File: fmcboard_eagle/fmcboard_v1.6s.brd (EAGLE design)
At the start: 147 x 74 mm, 297 parts, among them IC1 OPA699ID, IC10 LM358, IC11 7805DT, IC12 SN74AUC2G66DCTR, IC13 SN74AUC2G66DCTR, IC14 SN74AUC2G66DCTR, IC15 SN74AUC2G66DCTR, IC16 DAC7578SPWR, IC17 SN74AUC2G66DCTR, IC18 SN74AUC2G66DCTR, IC19 SN74AUC2G66DCTR, IC2 DAC7578SPWR, IC20 SN74AUC2G66DCTR, IC21 74AUP2GU04GW, IC22 74AUP2GU04GW, IC23 74AUP2GU04GW, IC24 74AUP2GU04GW, IC25 MC7905ACD2TR4G, IC26 AMS1117-1.8, IC27 LM358, IC28 SN74AUC2G66DCTR, IC29 LM337KVURG3, IC3 LTC6229IMS8E#TRPBF, IC30 SN74AUC2G66DCTR, IC31 SN74AUC2G66DCTR, IC32 SN74AUC2G66DCTR, IC33 LTC6229IMS8E#TRPBF, IC34 74AUP2GU04GW, IC35 74AUP2GU04GW, IC36 TPS5430DDAR, IC37 TPS5430DDAR, IC4 OPA695IDR, IC5 LTC6229IMS8E#TRPBF, IC6 OPA695IDR, IC7 OPA699ID, IC8 LM358, IC9 LM358, J1 8pin, J12 4p-2.54, J13 4p-2.54, J2 ASP-134604-01, J3 2p-2.54, J5 4p-2.54, J8 4p-2.54, J9 2p-2.54

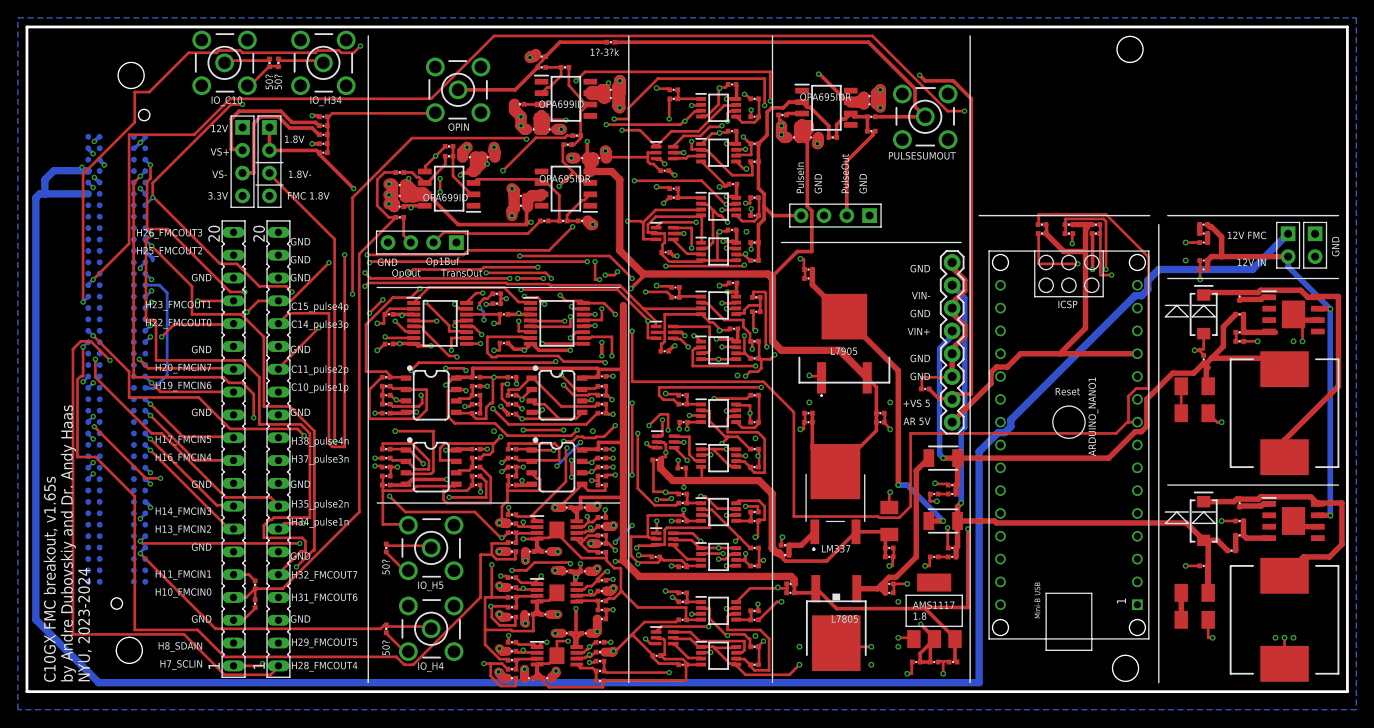
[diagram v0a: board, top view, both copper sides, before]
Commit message: extra 10 uF caps
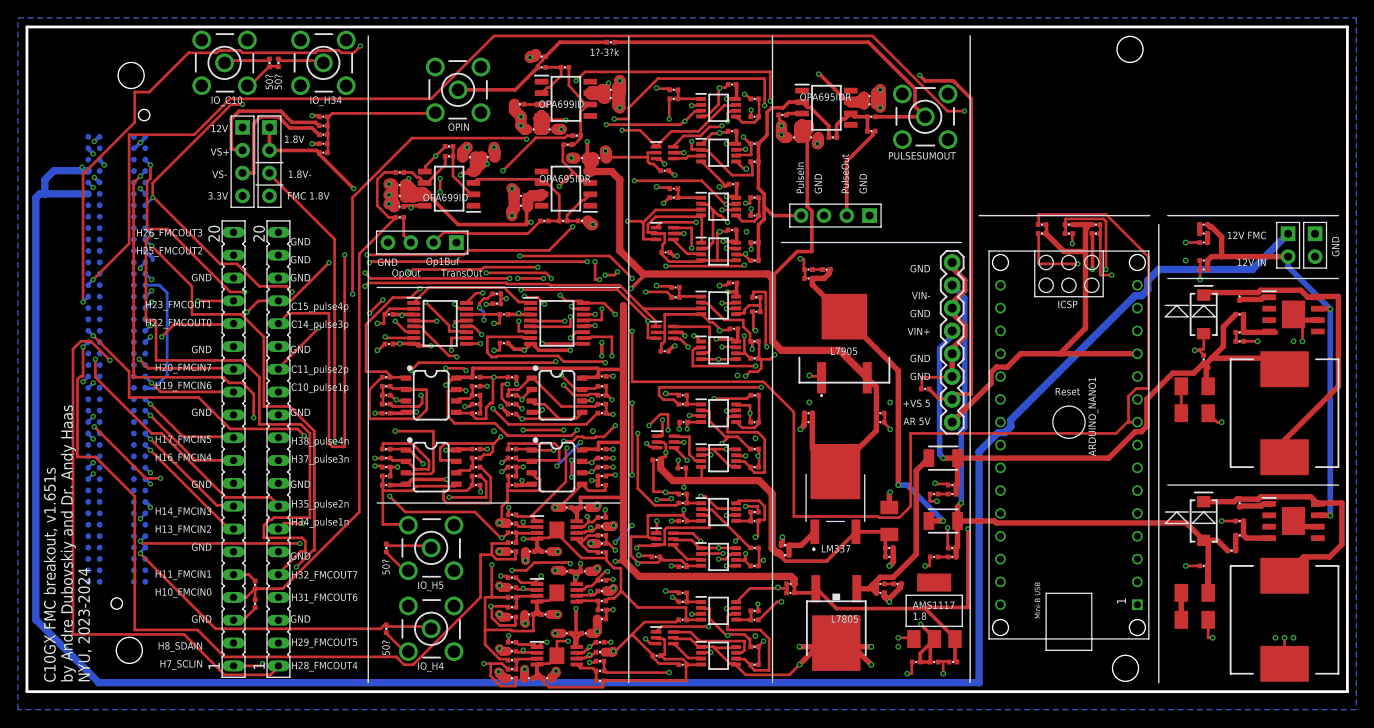
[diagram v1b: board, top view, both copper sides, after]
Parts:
- added C110, C111: 10uF, passives:0402_CAP
- moved C2 1.00 mm to (95.0, 12.0)
- moved C43 1.00 mm to (95.0, 11.0)
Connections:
- new net N$58: C110.1, C2.2
- new net N$59: C111.1, C40.2
- net GND: now also C110.2; no longer C2.2
- net VIN-CLEAN: now also C111.2; no longer C40.2
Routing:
- net GND: track 510.0 -> 529.4 mm, vias 136 -> 135
- net VS-: track 240.4 -> 252.4 mm
- net VIN-CLEAN: track 36.2 -> 37.8 mm
- net N$59: track 0.00 -> 1.13 mm
- net N$58: track 0.00 -> 1.03 mm
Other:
- board text added: "C10GX FMC breakout, v1.651s by Andre Dubovskiy and Dr. Andy Haas NYU, 2023-2024"
- board text removed: "C10GX FMC breakout, v1.65s by Andre Dubovskiy and Dr. Andy Haas NYU, 2023-2024"

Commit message: v1.652s Add C18 C19 C22 C23 pulse out holes Add C26 C27 SDAIN SCLIN holes
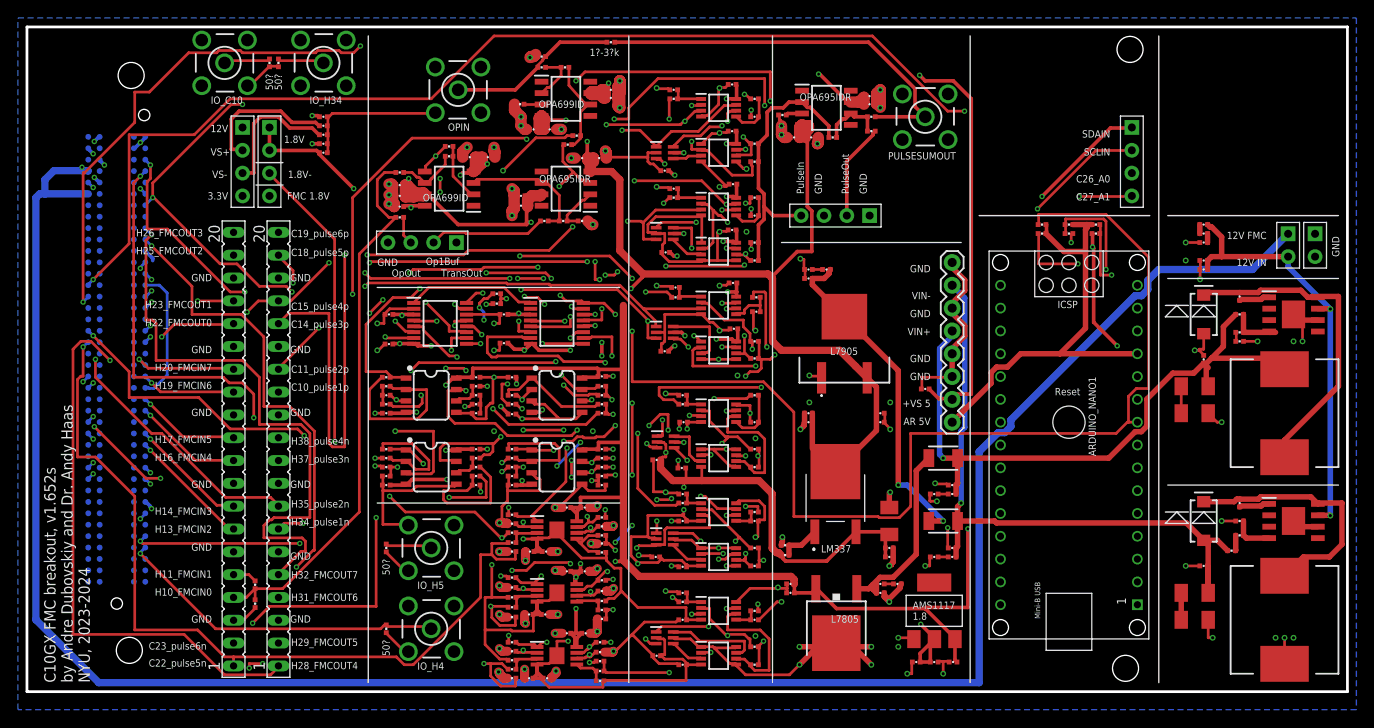
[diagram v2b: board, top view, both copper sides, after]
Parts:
- added J4: 4p-2.54, Seeed-Connector:H4-2.54
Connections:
- net C18: now also SV2.19
- net C19: now also SV2.20
- net C22: now also SV1.1
- net C23: now also SV1.2
- net C26: now also J4.3
- net C27: now also J4.4
- net GND: no longer SV2.19, SV2.20
- net SCLIN: now also J4.2; no longer SV1.1
- net SDAIN: now also J4.1; no longer SV1.2
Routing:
- net C23: track 74.4 -> 105.3 mm, vias 3 -> 5
- net SDAIN: track 153.7 -> 180.0 mm, vias 2 -> 4
- net SCLIN: track 156.9 -> 172.9 mm, vias 3 -> 5
- net C27: track 173.3 -> 181.5 mm, vias 2 -> 3
- net C19: track 85.3 -> 91.1 mm
- net C26: track 183.5 -> 189.0 mm
- net C18: track 76.8 -> 80.9 mm, vias 2 -> 3
- net C22: track 92.5 -> 93.5 mm
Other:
- board text added: "C10GX FMC breakout, v1.652s by Andre Dubovskiy and Dr. Andy Haas NYU, 2023-2024"
- board text added: "C18_pulse5p"
- board text added: "C19_pulse6p"
- board text added: "C22_pulse5n"
- board text added: "C23_pulse6n"
- board text added: "C26_A0"
- board text added: "C27_A1"
- board text added: "SCLIN"
- board text added: "SDAIN"
- board text removed: "C10GX FMC breakout, v1.651s by Andre Dubovskiy and Dr. Andy Haas NYU, 2023-2024"
- board text removed: "H7_SCLIN"
- board text removed: "H8_SDAIN"

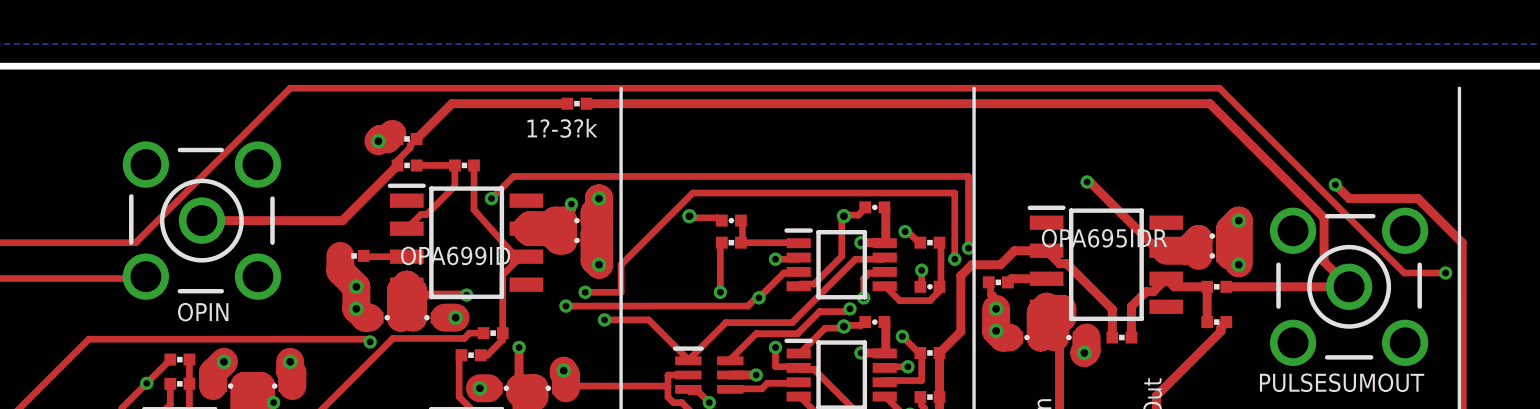
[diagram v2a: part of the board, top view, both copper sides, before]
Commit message: v1.652s 0805 test resistor instead of 0402
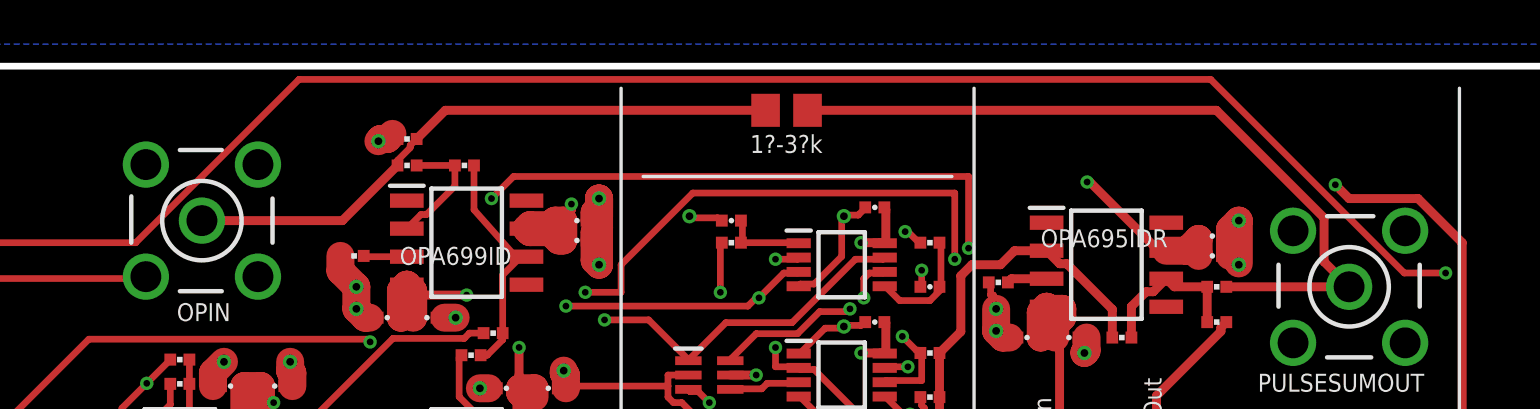
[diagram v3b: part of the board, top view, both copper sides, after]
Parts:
- R9: device passives:0402_RES -> rcl:R0805
- moved R9 9.50 mm to (74.5, 72.0)
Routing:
- net PULSEOUT: track 44.7 -> 34.6 mm
- net IO1: track 19.0 -> 27.8 mm
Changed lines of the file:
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@@
 <text x="120.6" y="57.5" size="0.8128" layer="21" rot="R180">C26_A0</text>
 <text x="120.6" y="55.5" size="0.8128" layer="21" rot="R180">C27_A1</text>
+<wire x1="68" y1="69" x2="82" y2="69" width="0.1524" layer="21"/>
 </plain>
 <attributes>
@@
 <attribute name="VALUE" x="59.5" y="65.4" size="0.8128" layer="21" align="center"/>
 </element>
-<element name="R9" library="passives" package="0402_RES" value="1?-3?k" x="65" y="72.3" smashed="yes">
-<attribute name="VALUE" x="65.932" y="71.581" size="0.8128" layer="21" ratio="15" rot="R180"/>
+<element name="R9" library="rcl" library_urn="urn:adsk.eagle:library:334" package="R0805" package3d_urn="urn:adsk.eagle:package:23553/2" value="1?-3?k" x="74.5" y="72" smashed="yes">
+<attribute name="POPULARITY" value="85" x="74.5" y="72" size="1.778" layer="27" display="off"/>
+<attribute name="SPICEPREFIX" value="R" x="74.5" y="72" size="1.778" layer="27" display="off"/>
+<attribute name="VALUE" x="76.132" y="70.881" size="0.8128" layer="21" ratio="15" rot="R180"/>
 </element>
 <element name="R10" library="passives" package="0402_RES" value="100" x="25.4" y="9.8" smashed="yes" rot="R90"/>
@@
 <wire x1="54.36693125" y1="67" x2="56.86693125" y2="69.5" width="0.4064" layer="1"/>
 <wire x1="48" y1="67" x2="54.36693125" y2="67" width="0.4064" layer="1"/>
-<wire x1="57.73306875" y1="70.7" x2="59.33306875" y2="72.3" width="0.4064" layer="1"/>
-<wire x1="59.33306875" y1="72.3" x2="64.56693125" y2="72.3" width="0.4064" layer="1"/>
+<wire x1="57.73306875" y1="70.7" x2="59.03306875" y2="72" width="0.4064" layer="1"/>
+<wire x1="59.03306875" y1="72" x2="73.55" y2="72" width="0.4064" layer="1"/>
 </signal>
 <signal name="1V8" class="1" airwireshidden="yes">
@@
 <wire x1="98.8656" y1="65.1344" x2="100" y2="64" width="0.4064" layer="1"/>
 <wire x1="98.8656" y1="67.12221875" x2="98.8656" y2="65.1344" width="0.4064" layer="1"/>
-<wire x1="65.43306875" y1="72.3" x2="93.68781875" y2="72.3" width="0.4064" layer="1"/>
-<wire x1="93.68781875" y1="72.3" x2="98.8656" y2="67.12221875" width="0.4064" layer="1"/>
+<wire x1="75.45" y1="72" x2="93.98781875" y2="72" width="0.4064" layer="1"/>
+<wire x1="93.98781875" y1="72" x2="98.8656" y2="67.12221875" width="0.4064" layer="1"/>
 </signal>
 <signal name="TRANSIN">
@@
 <wire x1="22.625" y1="66" x2="18.625" y2="62" width="0.3048" layer="1"/>
 <wire x1="45" y1="66" x2="22.625" y2="66" width="0.3048" layer="1"/>
-<wire x1="52" y1="73" x2="45" y2="66" width="0.3048" layer="1"/>
-<wire x1="94.125" y1="73" x2="52" y2="73" width="0.3048" layer="1"/>
-<wire x1="102.5" y1="64.625" x2="94.125" y2="73" width="0.3048" layer="1"/>
+<wire x1="52.4" y1="73.4" x2="45" y2="66" width="0.3048" layer="1"/>
+<wire x1="93.725" y1="73.4" x2="52.4" y2="73.4" width="0.3048" layer="1"/>
+<wire x1="102.5" y1="64.625" x2="93.725" y2="73.4" width="0.3048" layer="1"/>
 <wire x1="104.375" y1="64.625" x2="102.5" y2="64.625" width="0.3048" layer="1"/>
 <wire x1="122.625" y1="46.375" x2="115.5" y2="53.5" width="0.3048" layer="15"/>

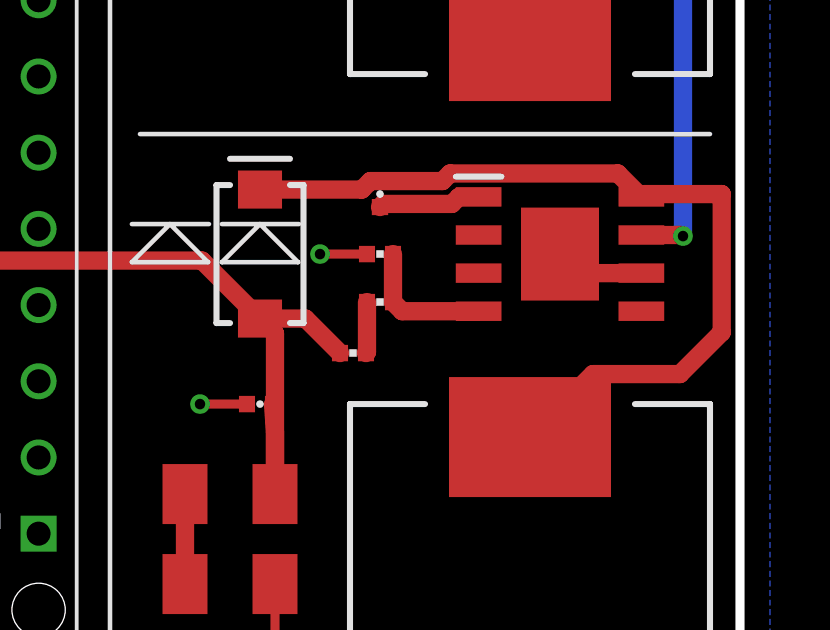
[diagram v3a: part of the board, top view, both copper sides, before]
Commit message: fix VIN-
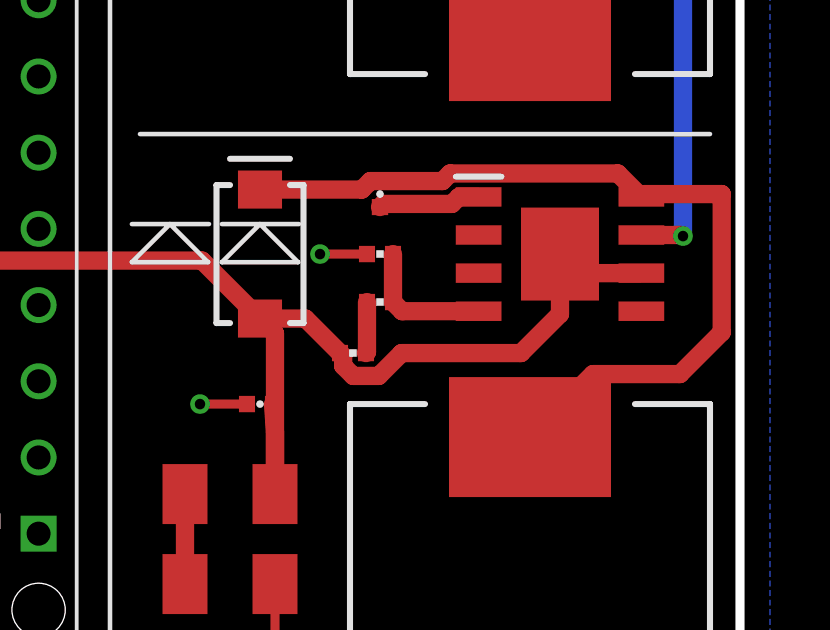
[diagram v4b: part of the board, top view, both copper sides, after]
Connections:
- removed net V-: IC36.6, IC36.9
- net VIN-: now also IC36.6, IC36.9
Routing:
- net VIN-: track 71.7 -> 85.4 mm
- net V-: track 2.98 -> 0.00 mm
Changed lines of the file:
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@@
 <wire x1="104.397" y1="29.4213375" x2="104.397" y2="43.843" width="0.6096" layer="16"/>
 <wire x1="104.397" y1="43.843" x2="103" y2="45.24" width="0.6096" layer="16"/>
+<contactref element="IC36" pad="6"/>
+<contactref element="IC36" pad="9"/>
+<wire x1="143.712" y1="18.365" x2="141.635" y2="18.365" width="0.6096" layer="1"/>
+<wire x1="141.635" y1="18.365" x2="141" y2="19" width="0.6096" layer="1"/>
+<wire x1="133.66693125" y1="15.7" x2="133.77106875" y2="15.5958625" width="0.6096" layer="1"/>
+<wire x1="135.72066875" y1="15.7" x2="139.7" y2="15.7" width="0.6096" layer="1"/>
+<wire x1="133.77106875" y1="15.5958625" x2="133.77106875" y2="15.2744" width="0.6096" layer="1"/>
+<wire x1="133.77106875" y1="15.2744" x2="134.10746875" y2="14.938" width="0.6096" layer="1"/>
+<wire x1="134.10746875" y1="14.938" x2="134.95866875" y2="14.938" width="0.6096" layer="1"/>
+<wire x1="134.95866875" y1="14.938" x2="135.72066875" y2="15.7" width="0.6096" layer="1"/>
+<wire x1="141" y1="17" x2="141" y2="19" width="0.6096" layer="1"/>
+<wire x1="139.7" y1="15.7" x2="141" y2="17" width="0.6096" layer="1"/>
 </signal>
 <signal name="DACP2">
@@
 <via x="59.5" y="35.25" extent="1-16" drill="0.3048"/>
 </signal>
-<signal name="V-">
-<contactref element="IC36" pad="6"/>
-<contactref element="IC36" pad="9"/>
-<wire x1="143.712" y1="18.365" x2="141.635" y2="18.365" width="0.6096" layer="1"/>
-<wire x1="141.635" y1="18.365" x2="141" y2="19" width="0.6096" layer="1"/>
-</signal>
 <signal name="SW2">
